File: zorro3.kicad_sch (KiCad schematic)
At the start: 0 parts

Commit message: Start populating Zorro III
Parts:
- added CN1: Zorro3, symbol Zorro3:Zorro3
- added U1, U2, U3: CY74FCT16543TPVCT, DL56, symbol 74FCT16543:CY74FCT16543TPVCT
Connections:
- new net A16: U3.5 (1A1)
- new net A17: U3.6 (1A2)
- new net A18: U3.8 (1A3)
- new net A19: U3.9 (1A4)
- new net A20: U3.10 (1A5)
- new net A21: U3.12 (1A6)
- new net A22: U3.13 (1A7)
- new net A23: U3.14 (1A8)
- new net A24: U3.15 (2A1)
- new net A25: U3.16 (2A2)
- new net A26: U3.17 (2A3)
- new net A27: U3.19 (2A4)
- new net A28: U3.20 (2A5)
- new net A29: U3.21 (2A6)
- new net A30: U3.23 (2A7)
- new net A31: U3.24 (2A8)
- new net ABOEH: U3.1 (*1OEAB), U3.28 (*2OEAB), U3.29 (*2OEBA), U3.56 (*1OEBA)
- new net BMASTER: U3.31 (*2CEBA), U3.54 (*1CEBA)
- new net D0: U1.5 (1A1)
- new net D1: U1.6 (1A2)
- new net D10: U1.17 (2A3)
- new net D11: U1.19 (2A4)
- new net D12: U1.20 (2A5)
- new net D13: U1.21 (2A6)
- new net D14: U1.23 (2A7)
- new net D15: U1.24 (2A8)
- new net D16: U2.5 (1A1)
- new net D17: U2.6 (1A2)
- new net D18: U2.8 (1A3)
- new net D19: U2.9 (1A4)
- new net D2: U1.8 (1A3)
- new net D20: U2.10 (1A5)
- new net D21: U2.12 (1A6)
- new net D22: U2.13 (1A7)
- new net D23: U2.14 (1A8)
- new net D24: U2.15 (2A1)
- new net D25: U2.16 (2A2)
- new net D26: U2.17 (2A3)
- new net D27: U2.19 (2A4)
- new net D28: U2.20 (2A5)
- new net D29: U2.21 (2A6)
- new net D2Z: U1.26 (*2CEAB), U1.3 (*1CEAB), U2.26 (*2CEAB), U2.3 (*1CEAB)
- new net D3: U1.9 (1A4)
- new net D30: U2.23 (2A7)
- new net D31: U2.24 (2A8)
- new net D4: U1.10 (1A5)
- new net D5: U1.12 (1A6)
- new net D6: U1.13 (1A7)
- new net D7: U1.14 (1A8)
- new net D8: U1.15 (2A1)
- new net D9: U1.16 (2A2)
- new net DBLT: U1.2 (*1LEAB), U1.27 (*2LEAB), U1.30 (*2LEBA), U1.55 (*1LEBA), U2.2 (*1LEAB), U2.27 (*2LEAB), U2.30 (*2LEBA), U2.55 (*1LEBA)
- new net DBOE: U1.1 (*1OEAB), U1.28 (*2OEAB), U1.29 (*2OEBA), U1.56 (*1OEBA), U2.1 (*1OEAB), U2.28 (*2OEAB), U2.29 (*2OEBA), U2.56 (*1OEBA)
- new net GND: U1.11 (GND), U1.18 (GND), U1.25 (GND), U1.32 (GND), U1.39 (GND), U1.4 (GND), U1.46 (GND), U1.53 (GND), U2.11 (GND), U2.18 (GND), U2.25 (GND), U2.32 (GND), U2.39 (GND), U2.4 (GND), U2.46 (GND), U2.53 (GND), U3.11 (GND), U3.18 (GND), U3.2 (*1LEAB), U3.25 (GND), U3.27 (*2LEAB), U3.32 (GND), U3.39 (GND), U3.4 (GND), U3.46 (GND), U3.53 (GND)
- new net MASTER: U3.26 (*2CEAB), U3.3 (*1CEAB)
- new net PLD_FCS: U3.30 (*2LEBA), U3.55 (*1LEBA)
- new net V5: U1.22 (VCC), U1.35 (VCC), U1.50 (VCC), U1.7 (VCC), U2.22 (VCC), U2.35 (VCC), U2.50 (VCC), U2.7 (VCC), U3.22 (VCC), U3.35 (VCC), U3.50 (VCC), U3.7 (VCC)
- new net Z2D: U1.31 (*2CEBA), U1.54 (*1CEBA), U2.31 (*2CEBA), U2.54 (*1CEBA)
- new net Z_A10D2: U1.49 (1B3)
- new net Z_A11D3: U1.48 (1B4)
- new net Z_A12D4: U1.47 (1B5)
- new net Z_A13D5: U1.45 (1B6)
- new net Z_A14D6: U1.44 (1B7)
- new net Z_A15D7: U1.43 (1B8)
- new net Z_A16D8: U1.42 (2B1), U3.52 (1B1)
- new net Z_A17D9: U1.41 (2B2), U3.51 (1B2)
- new net Z_A18D10: U1.40 (2B3), U3.49 (1B3)
- new net Z_A19D11: U1.38 (2B4), U3.48 (1B4)
- new net Z_A20D12: U1.37 (2B5), U3.47 (1B5)
- new net Z_A21D13: U1.36 (2B6), U3.45 (1B6)
- new net Z_A22D14: U1.34 (2B7), U3.44 (1B7)
- new net Z_A23D15: U1.33 (2B8), U3.43 (1B8)
- new net Z_A24D24: U2.42 (2B1), U3.42 (2B1)
- new net Z_A25D25: U2.41 (2B2), U3.41 (2B2)
- new net Z_A26D26: U2.40 (2B3), U3.40 (2B3)
- new net Z_A27D27: U2.38 (2B4), U3.38 (2B4)
- new net Z_A28D28: U2.37 (2B5), U3.37 (2B5)
- new net Z_A29D29: U2.36 (2B6), U3.36 (2B6)
- new net Z_A30D30: U2.34 (2B7), U3.34 (2B7)
- new net Z_A31D31: U2.33 (2B8), U3.33 (2B8)
- new net Z_A8D0: U1.52 (1B1)
- new net Z_A9D1: U1.51 (1B2)
- new net Z_D16: U2.52 (1B1)
- new net Z_D17: U2.51 (1B2)
- new net Z_D18: U2.49 (1B3)
- new net Z_D19: U2.48 (1B4)
- new net Z_D20: U2.47 (1B5)
- new net Z_D21: U2.45 (1B6)
- new net Z_D22: U2.44 (1B7)
- new net Z_D23: U2.43 (1B8)
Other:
- note added: "U100 / U101"
- note added: "U107 / U106"
- note added: "U108 / U105"

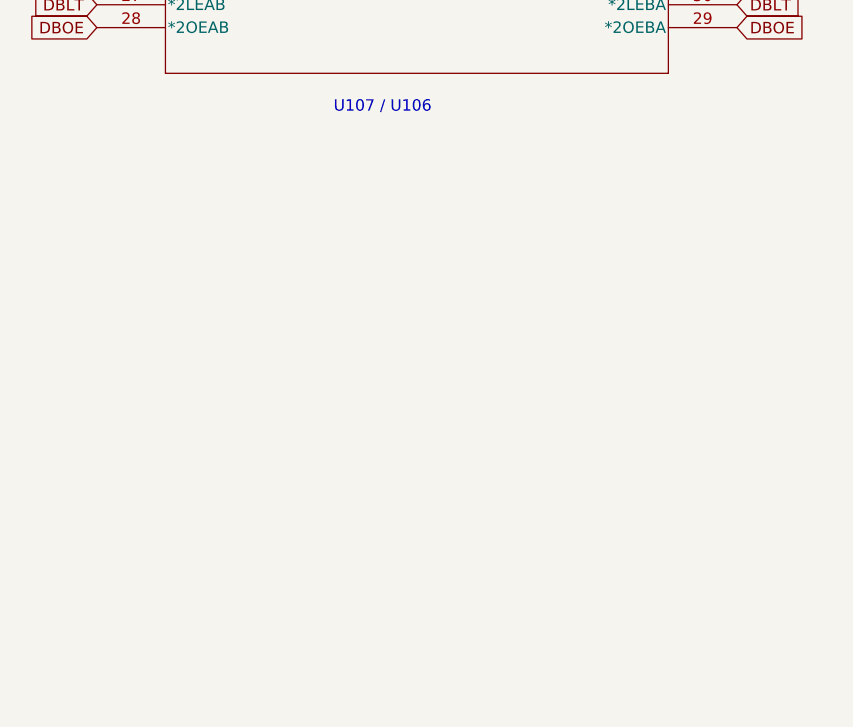
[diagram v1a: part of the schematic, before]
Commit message: Place CPLD, NCR and last 543 (Latched Trabceiver)
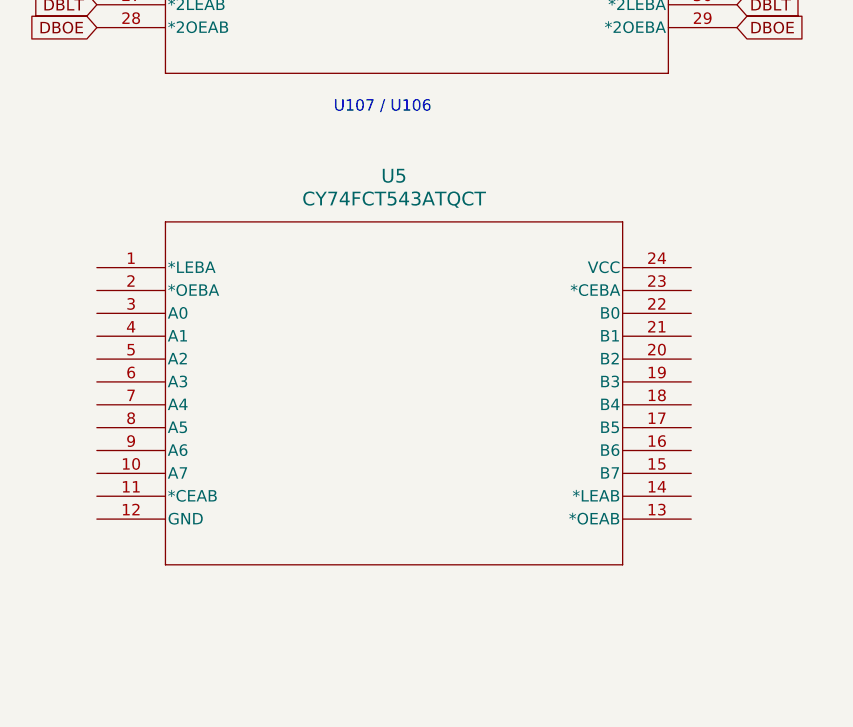
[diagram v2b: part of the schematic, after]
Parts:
- added U5: CY74FCT543ATQCT, DBQ24, symbol CY74FCT543ATQCT:CY74FCT543ATQCT
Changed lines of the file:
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@@
+	)
+	(symbol
+		(lib_id "CY74FCT543ATQCT:CY74FCT543ATQCT")
+		(at 27.94 123.19 0)
+		(unit 1)
+		(exclude_from_sim no)
+		(in_bom yes)
+		(on_board yes)
+		(dnp no)
+		(fields_autoplaced yes)
+		(property "Reference" "U5"
+			(at 60.96 113.03 0)
+			(effects
+				(font
+					(size 1.524 1.524)
+				)
+			)
+		)
+		(property "Value" "CY74FCT543ATQCT"
+			(at 60.96 115.57 0)
+			(effects
+				(font
+					(size 1.524 1.524)
+				)
+			)
+		)
+		(property "Footprint" "DBQ24"
+			(at 27.94 123.19 0)
+			(effects
+				(font
+					(size 1.27 1.27)
+					(italic yes)
+				)
+				(hide yes)
+			)
+		)
+		(property "Datasheet" "CY74FCT543ATQCT"
+			(at 27.94 123.19 0)
+			(effects
+				(font
+					(size 1.27 1.27)
+					(italic yes)
+				)
+				(hide yes)
+			)
+		)
+		(property "Description" ""
+			(at 27.94 123.19 0)
+			(effects
+				(font
+					(size 1.27 1.27)
+				)
+				(hide yes)
+			)
+		)
+		(pin "13"
+		)
+		(pin "17"
+		)
+		(pin "9"
+		)
+		(pin "21"
+		)
+		(pin "2"
+		)
+		(pin "4"
+		)
+		(pin "10"
+		)
+		(pin "15"
+		)
+		(pin "20"
+		)
+		(pin "11"
+		)
+		(pin "3"
+		)
+		(pin "1"
+		)
+		(pin "6"
+		)
+		(pin "5"
+		)
+		(pin "8"
+		)
+		(pin "23"
+		)
+		(pin "24"
+		)
+		(pin "12"
+		)
+		(pin "7"
+		)
+		(pin "18"
+		)
+		(pin "14"
+		)
+		(pin "19"
+		)
+		(pin "22"
+		)
+		(pin "16"
+		)
+		(instances
+			(project ""
+				(path "/8f9f4021-47aa-41d9-bea7-f6ccf72098bb/54ff82a5-3c96-49ab-8139-25683e385401"
+					(reference "U5")
+					(unit 1)
+				)
+			)
+		)
 	)
 	(symbol

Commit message: Update design
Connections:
- net ABOEH: now also U5.2 (*OEBA)
- net BMASTER: now also U5.23 (*CEBA)
- net GND: now also CN1.1 (GND), CN1.100 (GND), CN1.13 (GND), CN1.2 (GND), CN1.25 (GND), CN1.3 (GND), CN1.37 (GND), CN1.4 (GND), CN1.49 (GND), CN1.61 (GND), CN1.73 (GND), CN1.85 (GND), CN1.87 (GND), CN1.88 (GND), CN1.89 (GND), CN1.90 (GND), CN1.91 (GND), CN1.99 (GND), U5.12 (GND), U5.14 (*LEAB)
- net MASTER: now also U5.11 (*CEAB)
- net PLD_FCS: now also U5.1 (*LEBA)
- net V5: now also CN1.5 (+5), CN1.6 (+5), U5.24 (VCC)
- net Z_A10D2: now also CN1.34 (A10/A10+D2), U5.17 (B5)
- net Z_A11D3: now also CN1.36 (A11/A11+D3), U5.18 (B4)
- net Z_A12D4: now also CN1.38 (A12/A12+D4), U5.19 (B3)
- net Z_A13D5: now also CN1.39 (A13/A13+D5), U5.20 (B2)
- net Z_A14D6: now also CN1.41 (A14/A14+D6), U5.21 (B1)
- net Z_A15D7: now also CN1.43 (A15/A15+D7), U5.22 (B0)
- net Z_A16D8: now also CN1.45 (A16/A16+D8)
- net Z_A17D9: now also CN1.47 (A17/A17+D9)
- net Z_A18D10: now also CN1.52 (A18/A18+D10)
- net Z_A19D11: now also CN1.54 (A19/A19+D11)
- net Z_A20D12: now also CN1.56 (A20/A20+D12)
- net Z_A21D13: now also CN1.58 (A21/A21+D13)
- net Z_A22D14: now also CN1.57 (A22/A22+D14)
- net Z_A23D15: now also CN1.59 (A23/A23+D15)
- net Z_A24D24: now also CN1.80 (D8/A24+D24)
- net Z_A25D25: now also CN1.78 (D9/A25+D25)
- net Z_A26D26: now also CN1.76 (D10/A26+D26)
- net Z_A27D27: now also CN1.71 (D11/A27+D27)
- net Z_A28D28: now also CN1.69 (D12/A28+D28)
- net Z_A29D29: now also CN1.67 (D13/A29+D29)
- net Z_A30D30: now also CN1.65 (D14/A30+D30)
- net Z_A31D31: now also CN1.63 (D15/A31+D31)
- net Z_A8D0: now also CN1.30 (A8/A8+D0), U5.15 (B7)
- net Z_A9D1: now also CN1.32 (A9/A9+D1), U5.16 (B6)
- net Z_D16: now also CN1.75 (D0/RSVD+D16)
- net Z_D17: now also CN1.77 (D1/RSVD+D17)
- net Z_D18: now also CN1.79 (D2/RSVD+D18)
- net Z_D19: now also CN1.81 (D3/RSVD+D19)
- net Z_D20: now also CN1.83 (D4/RSVD+D20)
- net Z_D21: now also CN1.86 (D5/RSVD+D21)
- net Z_D22: now also CN1.84 (D6/RSVD+D22)
- net Z_D23: now also CN1.82 (D7/RSVD+D23)
- net A8: now reaches U5.10 (A7)
- net IORST: now reaches U5.13 (*OEAB)
- net A15: now reaches U5.3 (A0)
- net A14: now reaches U5.4 (A1)
- net A13: now reaches U5.5 (A2)
- net A12: now reaches U5.6 (A3)
- net A11: now reaches U5.7 (A4)
- net A10: now reaches U5.8 (A5)
- net A9: now reaches U5.9 (A6)
- net Z_CFGOUT: now reaches CN1.11 (~{CFGOUT})
- net Z_CFGIN: now reaches CN1.12 (~{CFGIN})
- net Z_CINH: now reaches CN1.17 (~{CINH}/~{OVR})
- net Z_MTCR: now reaches CN1.18 (XRDY/~{MTCR})
- net Z_INT2: now reaches CN1.19 (~{INT2})
- net Z_A5: now reaches CN1.21 (A5)
- net Z_A6: now reaches CN1.23 (A6)
- net Z_A4: now reaches CN1.24 (A4)
- net Z_A3: now reaches CN1.26 (A3)
- net Z_A2: now reaches CN1.27 (A2)
- net Z_A7: now reaches CN1.28 (A7)
- net Z_A1: now reaches CN1.29 (~{LOCK}/A1)
- net Z_FC0: now reaches CN1.31 (FC0)
- net Z_FC1: now reaches CN1.33 (FC1)
- net Z_FC2: now reaches CN1.35 (FC2)
- net Z_BEER: now reaches CN1.46 (~{BEER})
- net Z_MTACK: now reaches CN1.48 (VPA)
- net Z_DS0: now reaches CN1.51 (~{DS0}/~{VMA})
- net Z_BRn: now reaches CN1.60 (~{BRn})
- net Z_BGn: now reaches CN1.64 (~{BGn})
- net Z_DTACK: now reaches CN1.66 (~{DTACK})
- net Z_READ: now reaches CN1.68 (READ)
- net Z_DS2: now reaches CN1.70 (~{LDS}/~{DS2})
- net Z_DS3: now reaches CN1.72 (~{UDS}/~{DS3})
- net Z_SLAVE: now reaches CN1.9 (~{SLAVE})
- net Z_SENSEZ3: now reaches CN1.91 (GND/SenseZ3)
- net Z_7M: now reaches CN1.92 (7Mhz)
- net Z_DOE: now reaches CN1.93 (DOE)
- net Z_IORST: now reaches CN1.94 (~{BUSRST}/~{IORST})
- net Z_FCS: now reaches CN1.97 (NC/~{FCS})
- net Z_DS1: now reaches CN1.98 (NC/~{DS1})
- net V12: now reaches CN1.10 (+12)
- no-connect marks 0 -> 17

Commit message: More work. Getting there.
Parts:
- added C5: 10pF, symbol Device:C_Small
- added R12, R13, R14, R15, R16: 1K, YC324-FK-071KL:RESCAXS127P508X320X70-8N, symbol YC324-FK-071KL:YC324-FK-071KL
- added U11: SN74ABT16374ADGGR, DGG48, symbol SN74ABT16374ADGGR:SN74ABT16374ADGGR
- added U12: 74LVC07APW_118, TSSOP14_5P1X4P5_NEX, symbol 74LVC07APW_118:74LVC07APW_118
- added U13: SN74ABT16245ADGGR, DGG48, symbol SN74ABT16245ADGGR:SN74ABT16245ADGGR
- added U14: 74ACT521MTCX, TSSOP20_4P4X6P5_ONS, symbol 74ACT521MTCX:74ACT521MTCX
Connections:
- net A24: now also U14.17 (A7)
- net A25: now also U14.15 (A6)
- net A26: now also U14.13 (A5)
- net A27: now also U14.11 (A4)
- net A28: now also U14.8 (A3)
- net A29: now also U14.6 (A2)
- net A30: now also U14.4 (A1)
- net A31: now also U14.2 (A0)
- net BMASTER: now also U13.1 (1DIR), U13.24 (2DIR)
- net D0: now also U11.26 (2D8)
- net D1: now also U11.22 (2Q7), U11.23 (2Q8), U11.27 (2D7)
- net D2: now also U11.20 (2Q6), U11.29 (2D6)
- net D24: now also U11.37 (1D8)
- net D25: now also U11.38 (1D7)
- net D26: now also U11.40 (1D6)
- net D27: now also U11.41 (1D5)
- net D28: now also U11.43 (1D4)
- net D29: now also U11.44 (1D3)
- net D3: now also U11.19 (2Q5), U11.30 (2D5)
- net D30: now also U11.46 (1D2)
- net D31: now also U11.47 (1D1)
- net D4: now also U11.17 (2Q4), U11.32 (2D4)
- net D5: now also U11.16 (2Q3), U11.33 (2D3)
- net D6: now also U11.14 (2Q2), U11.35 (2D2)
- net D7: now also U11.13 (2Q1), U11.36 (2D1)
- net GND: now also C5.2, R16.5, U11.10 (GND), U11.15 (GND), U11.21 (GND), U11.28 (GND), U11.34 (GND), U11.39 (GND), U11.4 (GND), U11.45 (GND), U12.11 (5A), U12.13 (6A), U12.7 (GND), U13.10 (GND), U13.15 (GND), U13.21 (GND), U13.28 (GND), U13.34 (GND), U13.39 (GND), U13.4 (GND), U13.45 (GND), U14.1 (*IA=B), U14.10 (GND)
- net IORST: now also U12.8 (4Y)
- net V5: now also R12.5, R12.6, R12.7, R12.8, R13.5, R13.6, R13.7, R13.8, R14.5, R14.6, R14.7, R14.8, R15.5, R15.6, R15.7, R15.8, R16.7, R16.8, U11.18 (VCC), U11.31 (VCC), U11.42 (VCC), U11.7 (VCC), U12.14 (VCC), U13.18 (VCC), U13.31 (VCC), U13.42 (VCC), U13.7 (VCC), U14.20 (VCC)
- net Z_A2: now also U13.9 (1B6)
- net Z_A3: now also U13.8 (1B5)
- net Z_A4: now also U13.6 (1B4)
- net Z_A5: now also U13.5 (1B3)
- net Z_A6: now also U13.3 (1B2)
- net Z_A7: now also U13.2 (1B1)
- net Z_CFGOUT: now also U11.1 (*1OE)
- net Z_DOE: now also U13.16 (2B3)
- net Z_DS0: now also U13.23 (2B8)
- net Z_DS1: now also U13.22 (2B7)
- net Z_DS2: now also U13.20 (2B6)
- net Z_DS3: now also U13.19 (2B5)
- net Z_DTACK: now also C5.1
- net Z_FC0: now also U13.14 (2B2)
- net Z_FC1: now also U13.13 (2B1)
- net Z_FC2: now also U13.11 (1B7)
- net Z_IORST: now also U12.9 (4A)
- net Z_MTCR: now also U13.17 (2B4)
- net Z_READ: now also U13.12 (1B8)
- new net A2: U13.40 (1A6)
- new net A3: U13.41 (1A5)
- new net A4: U13.43 (1A4)
- new net A5: U13.44 (1A3)
- new net A6: U13.46 (1A2)
- new net A7: U13.47 (1A1)
- new net ABOEL: U13.25 (*2OE), U13.48 (*1OE)
- new net BERR: U12.6 (3Y)
- new net LED: U12.2 (1Y), U12.4 (2Y)
- new net M24: R12.1, U11.12 (1Q8), U14.18 (B7)
- new net M25: R12.2, U11.11 (1Q7), U14.16 (B6)
- new net M26: R12.3, U11.9 (1Q6), U14.14 (B5)
- new net M27: R12.4, U11.8 (1Q5), U14.12 (B4)
- new net M28: R13.1, U11.6 (1Q4), U14.9 (B4)
- new net M29: R13.2, U11.5 (1Q3), U14.7 (B2)
- new net M30: R13.3, U11.3 (1Q2), U14.5 (B1)
- new net M31: R13.4, U11.2 (1Q1), U14.3 (B0)
- new net MATCH: U14.19 (*OA=B)
- new net PLD_CFGLT: U11.48 (1CLK)
- new net PLD_DOE: R16.4, U13.33 (2A3)
- new net PLD_DS0: R15.4
- new net PLD_DS1: R15.3, U13.26 (2A8), U13.27 (2A7)
- new net PLD_DS2: R15.2, U13.29 (2A6)
- new net PLD_DS3: R15.1, U13.30 (2A5)
- new net PLD_FC0: R14.4, U13.35 (2A2)
- new net PLD_FC1: R14.3, U13.36 (2A1)
- new net PLD_FC2: R14.1, U13.38 (1A7)
- new net PLD_INTREG: U11.25 (2CLK)
- new net PLD_INTVEC: U11.24 (*2OE)
- new net PLD_MTCR: R16.1, U13.32 (2A4)
- new net PLD_READ: R14.2, U13.37 (1A8)
- new net SCSI_BUSY: U12.1 (1A), U12.3 (2A)
- new net Z_BERR: U12.5 (3A)
- new net Z_SENSE3: R16.2
- no-connect marks 17 -> 22
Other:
- note added: "2x8bit register w/ 3state"
- note added: "Identity Comparator"
- note added: "Is this intentional?"
- note added: "TODO 1x374 + 521 move into CPLD"
- note added: "USE 74ABT16543 instead of 74FCT16543"
- note added: "Z_DS3 + Z_DS2 have FBs on original but not Z_DS1 and Z_DS0"
- moved on the sheet: CN1A, CN1B

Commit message: Latest updates
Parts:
- added FB4, FB5: 60, Capacitor_SMD:C_0603_1608Metric_Pad1.08x0.95mm_HandSolder, symbol Device:FerriteBead_Small
- C5: footprint (none) -> Capacitor_SMD:C_0603_1608Metric_Pad1.08x0.95mm_HandSolder
- CN1: footprint (none) -> Zorro3:Zorro3-CardEdge
- U1, U2, U3: footprint DL56 -> 74FCT16543:DL56
- U11: footprint DGG48 -> SN74ABT16374ADGGR:DGG48
- U12: footprint TSSOP14_5P1X4P5_NEX -> 74LVC07APW_118:TSSOP14_5P1X4P5_NEX
- U13: footprint DGG48 -> SN74ABT16245ADGGR:DGG48
- U14: footprint TSSOP20_4P4X6P5_ONS -> 74ACT521MTCX:TSSOP20_4P4X6P5_ONS
- U5: footprint DBQ24 -> 74FCT16543:DL56
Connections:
- net Z_DS2: now also FB5.2; no longer U13.20 (2B6)
- net Z_DS3: now also FB4.2; no longer U13.19 (2B5)
- new net: FB4.1, U13.19 (2B5)
- new net: FB5.1, U13.20 (2B6)
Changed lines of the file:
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@@
 	(wire
 		(pts
+			(xy 186.69 223.52) (xy 190.5 223.52)
+		)
+		(stroke
+			(width 0)
+			(type default)
+		)
+	)
+	(wire
+		(pts
 			(xy 35.56 217.17) (xy 38.1 217.17)
 		)
@@
 	(wire
 		(pts
+			(xy 180.34 223.52) (xy 181.61 223.52)
+		)
+		(stroke
+			(width 0)
+			(type default)
+		)
+	)
+	(wire
+		(pts
 			(xy 345.44 168.91) (xy 345.44 171.45)
 		)
@@
 	(wire
 		(pts
+			(xy 185.42 220.98) (xy 190.5 220.98)
+		)
+		(stroke
+			(width 0)
+			(type default)
+		)
+	)
+	(wire
+		(pts
 			(xy 345.44 166.37) (xy 345.44 168.91)
 		)
@@
 		)
 	)
-	(global_label "Z_DS3"
-		(shape input)
-		(at 190.5 220.98 180)
-		(fields_autoplaced yes)
-		(effects
-			(font
-				(size 1.27 1.27)
-			)
-			(justify right)
-		)
-		(property "Intersheetrefs" "${INTERSHEET_REFS}"
-			(at 181.6487 220.98 0)
-			(effects
-				(font
-					(size 1.27 1.27)
-				)
-				(justify right)
-				(hide yes)
-			)
-		)
-	)
 	(global_label "GND"
 		(shape input)
@@
 		)
 	)
+	(global_label "Z_DS2"
+		(shape input)
+		(at 180.34 223.52 180)
+		(fields_autoplaced yes)
+		(effects
+			(font
+				(size 1.27 1.27)
+			)
+			(justify right)
+		)
+		(property "Intersheetrefs" "${INTERSHEET_REFS}"
+			(at 171.4887 223.52 0)
+			(effects
+				(font
+					(size 1.27 1.27)
+				)
+				(justify right)
+				(hide yes)
+			)
+		)
+	)
 	(global_label "V5"
 		(shape input)
@@
 		)
 	)
+	(global_label "Z_DS3"
+		(shape input)
+		(at 180.34 220.98 180)
+		(fields_autoplaced yes)
+		(effects
+			(font
+				(size 1.27 1.27)
+			)
+			(justify right)
+		)
+		(property "Intersheetrefs" "${INTERSHEET_REFS}"
+			(at 171.4887 220.98 0)
+			(effects
+				(font
+					(size 1.27 1.27)
+				)
+				(justify right)
+				(hide yes)
+			)
+		)
+	)
 	(global_label "DBOE"
 		(shape input)
@@
 		)
 	)
-	(global_label "Z_DS2"
-		(shape input)
-		(at 190.5 223.52 180)
-		(fields_autoplaced yes)
-		(effects
-			(font
-				(size 1.27 1.27)
-			)
-			(justify right)
-		)
-		(property "Intersheetrefs" "${INTERSHEET_REFS}"
-			(at 181.6487 223.52 0)
-			(effects
-				(font
-					(size 1.27 1.27)
-				)
-				(justify right)
-				(hide yes)
-			)
-		)
-	)
 	(global_label "A8"
 		(shape input)
@@
 			)
 		)
-		(property "Footprint" "DL56"
+		(property "Footprint" "74FCT16543:DL56"
 			(at 226.06 26.67 0)
 			(effects
@@
 			)
 		)
-		(property "Footprint" "DBQ24"
+		(property "Footprint" "74FCT16543:DL56"
 			(at 27.94 123.19 0)
 			(effects
@@
 			)
 		)
-		(property "Footprint" ""
+		(property "Footprint" "Zorro3:Zorro3-CardEdge"
 			(at 472.44 22.86 0)
 			(effects
@@
 			)
 		)
-		(property "Footprint" "DL56"
+		(property "Footprint" "74FCT16543:DL56"
 			(at 27.94 27.94 0)
 			(effects
@@
 	)
 	(symbol
+		(lib_id "Device:FerriteBead_Small")
+		(at 182.88 220.98 270)
+		(unit 1)
+		(exclude_from_sim no)
+		(in_bom yes)
+		(on_board yes)
+		(dnp no)
+		(property "Reference" "FB4"
+			(at 182.88 218.44 90)
+			(effects
+				(font
+					(size 1.27 1.27)
+				)
+			)
+		)
+		(property "Value" "60"
+			(at 182.88 220.98 90)
+			(effects
+				(font
+					(size 0.762 0.762)
+				)
+			)
+		)
+		(property "Footprint" "Capacitor_SMD:C_0603_1608Metric_Pad1.08x0.95mm_HandSolder"
+			(at 182.88 219.202 90)
+			(effects
+				(font
+					(size 1.27 1.27)
+				)
+				(hide yes)
+			)
+		)
+		(property "Datasheet" "https://www.mouser.com/datasheet/2/281/QNFA9101-1915702.pdf"
+			(at 182.88 220.98 0)
+			(effects
+				(font
+					(size 1.27 1.27)
+				)
+				(hide yes)
+			)
+		)
+		(property "Description" "Ferrite bead, small symbol"
+			(at 182.88 220.98 0)
+			(effects
+				(font
+					(size 1.27 1.27)
+				)
+				(hide yes)
+			)
+		)
+		(pin "1"
+		)
+		(pin "2"
+		)
+		(instances
+			(project "A4092"
+				(path "/8f9f4021-47aa-41d9-bea7-f6ccf72098bb/54ff82a5-3c96-49ab-8139-25683e385401"
+					(reference "FB4")
+					(unit 1)
+				)
+			)
+		)
+	)
+	(symbol
 		(lib_id "74LVC07APW_118:74LVC07APW_118")
 		(at 344.17 220.98 0)
@@
 			)
 		)
-		(property "Footprint" "TSSOP14_5P1X4P5_NEX"
+		(property "Footprint" "74LVC07APW_118:TSSOP14_5P1X4P5_NEX"
 			(at 344.17 220.98 0)
 			(effects
@@
 			)
 		)
-		(property "Footprint" "TSSOP20_4P4X6P5_ONS"
+		(property "Footprint" "74ACT521MTCX:TSSOP20_4P4X6P5_ONS"
 			(at 22.86 181.61 0)
 			(effects
@@
 			)
 		)
-		(property "Footprint" ""
+		(property "Footprint" "Zorro3:Zorro3-CardEdge"
 			(at 471.17 113.03 0)
 			(effects
@@
 			)
 		)
-		(property "Footprint" ""
+		(property "Footprint" "Capacitor_SMD:C_0603_1608Metric_Pad1.08x0.95mm_HandSolder"
 			(at 322.58 49.53 0)
 			(effects
@@
 			)
 		)
-		(property "Footprint" "DGG48"
+		(property "Footprint" "SN74ABT16245ADGGR:DGG48"
 			(at 190.5 175.26 0)
 			(effects
@@
 			)
 		)
-		(property "Footprint" "DGG48"
+		(property "Footprint" "SN74ABT16374ADGGR:DGG48"
 			(at 88.9 175.26 0)
 			(effects
@@
 	)
 	(symbol
+		(lib_id "Device:FerriteBead_Small")
+		(at 184.15 223.52 270)
+		(unit 1)
+		(exclude_from_sim no)
+		(in_bom yes)
+		(on_board yes)
+		(dnp no)
+		(property "Reference" "FB5"
+			(at 187.452 222.504 90)
+			(effects
+				(font
+					(size 1.27 1.27)
+				)
+			)
+		)
+		(property "Value" "60"
+			(at 184.15 223.52 90)
+			(effects
+				(font
+					(size 0.762 0.762)
+				)
+			)
+		)
+		(property "Footprint" "Capacitor_SMD:C_0603_1608Metric_Pad1.08x0.95mm_HandSolder"
+			(at 184.15 221.742 90)
+			(effects
+				(font
+					(size 1.27 1.27)
+				)
+				(hide yes)
+			)
+		)
+		(property "Datasheet" "https://www.mouser.com/datasheet/2/281/QNFA9101-1915702.pdf"
+			(at 184.15 223.52 0)
+			(effects
+				(font
+					(size 1.27 1.27)
+				)
+				(hide yes)
+			)
+		)
+		(property "Description" "Ferrite bead, small symbol"
+			(at 184.15 223.52 0)
+			(effects
+				(font
+					(size 1.27 1.27)
+				)
+				(hide yes)
+			)
+		)
+		(pin "1"
+		)
+		(pin "2"
+		)
+		(instances
+			(project "A4092"
+				(path "/8f9f4021-47aa-41d9-bea7-f6ccf72098bb/54ff82a5-3c96-49ab-8139-25683e385401"
+					(reference "FB5")
+					(unit 1)
+				)
+			)
+		)
+	)
+	(symbol
 		(lib_id "74FCT16543:CY74FCT16543TPVCT")
 		(at 125.73 26.67 0)
@@
 			)
 		)
-		(property "Footprint" "DL56"
+		(property "Footprint" "74FCT16543:DL56"
 			(at 125.73 26.67 0)
 			(effects
